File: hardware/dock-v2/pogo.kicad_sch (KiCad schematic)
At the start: 17 parts, among them J601 Pogo 7-pin, Q601 2N7002, Q602 2N7002, U601 TPD4E1U06DBVR, U602 SY6280AAC

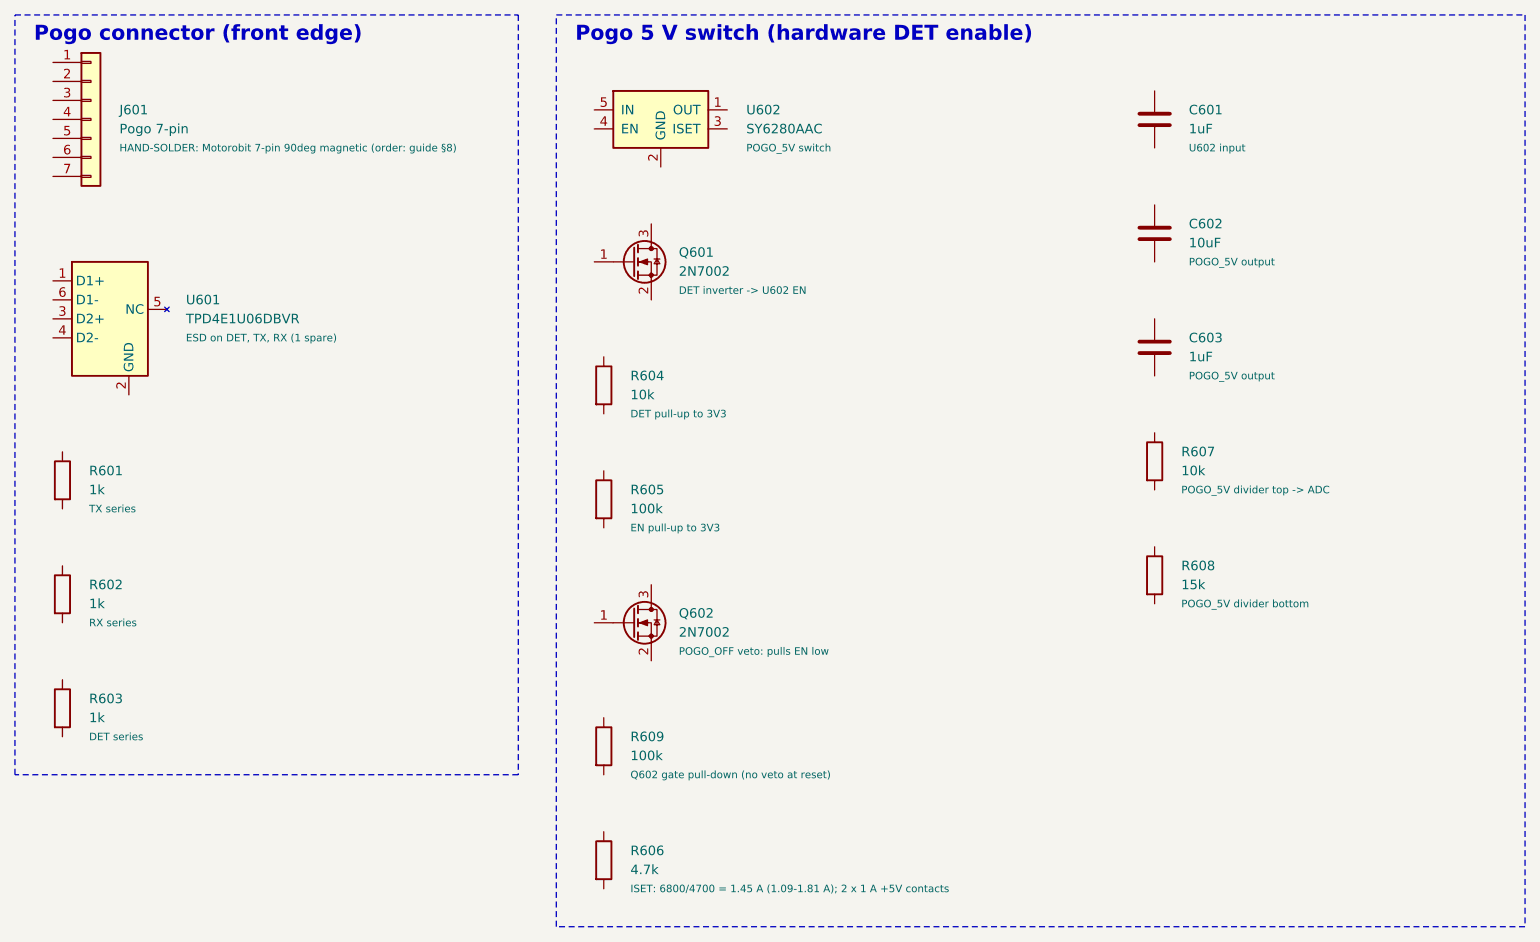
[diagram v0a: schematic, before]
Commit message: Dock v2 schematic: wiring in progress (user's work, snapshot before fixes)
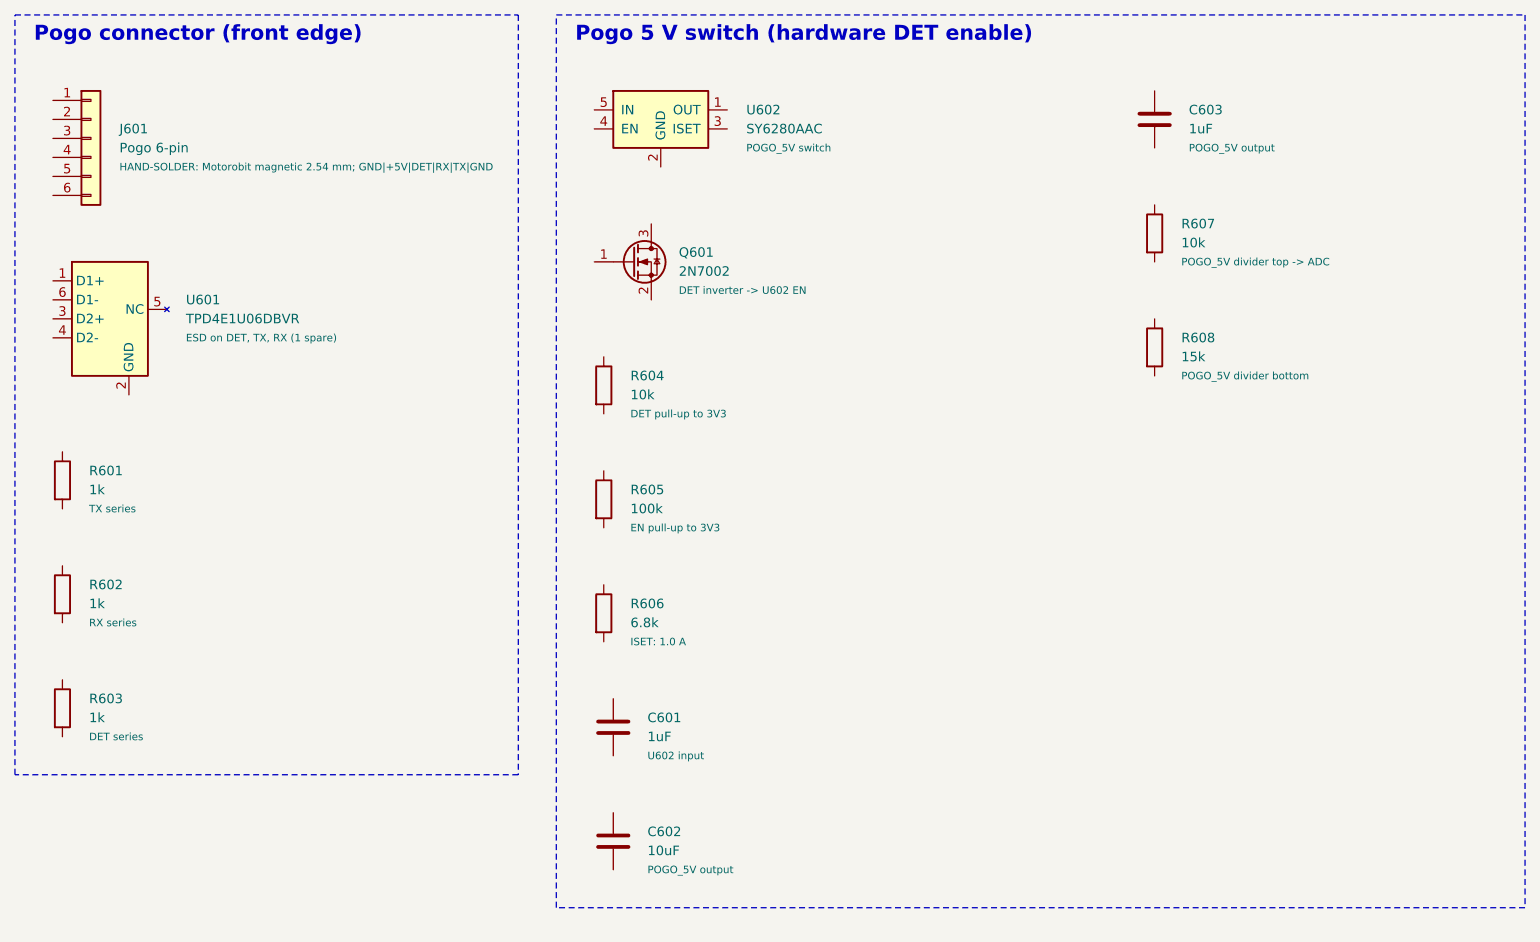
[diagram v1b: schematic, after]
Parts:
- removed J601: Pogo 7-pin, dock:Pogo-7, symbol Connector_Generic:Conn_01x07
- removed Q602: 2N7002, Package_TO_SOT_SMD:SOT-23, symbol Transistor_FET:2N7002
- removed R609: 100k, Resistor_SMD:R_0402_1005Metric, symbol Device:R
- added J601: Pogo 6-pin, dock:Pogo-6, symbol Connector_Generic:Conn_01x06
- R606: value 4.7k -> 6.8k; LCSC C25900 -> C25917; Note ISET: 6800/4700 = 1.45 A (1.09-1.81 A); 2 x 1 A +5V contacts -> ISET: 1.0 A
